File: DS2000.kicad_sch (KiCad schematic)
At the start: 56 parts, among them J1 USB-C, J2 SWD, J3 USB wire, SW1 MUTE, SW2 DEAFEN, SW3 DISCONNECT, SW4 BOOTSEL, SW5 RESET, U1 USBLC6-2SC6, U2 AP2112K-3.3, U3 RP2350A, U4 W25Q32JVSS, U5 74AHCT1G125, Y1 12MHz

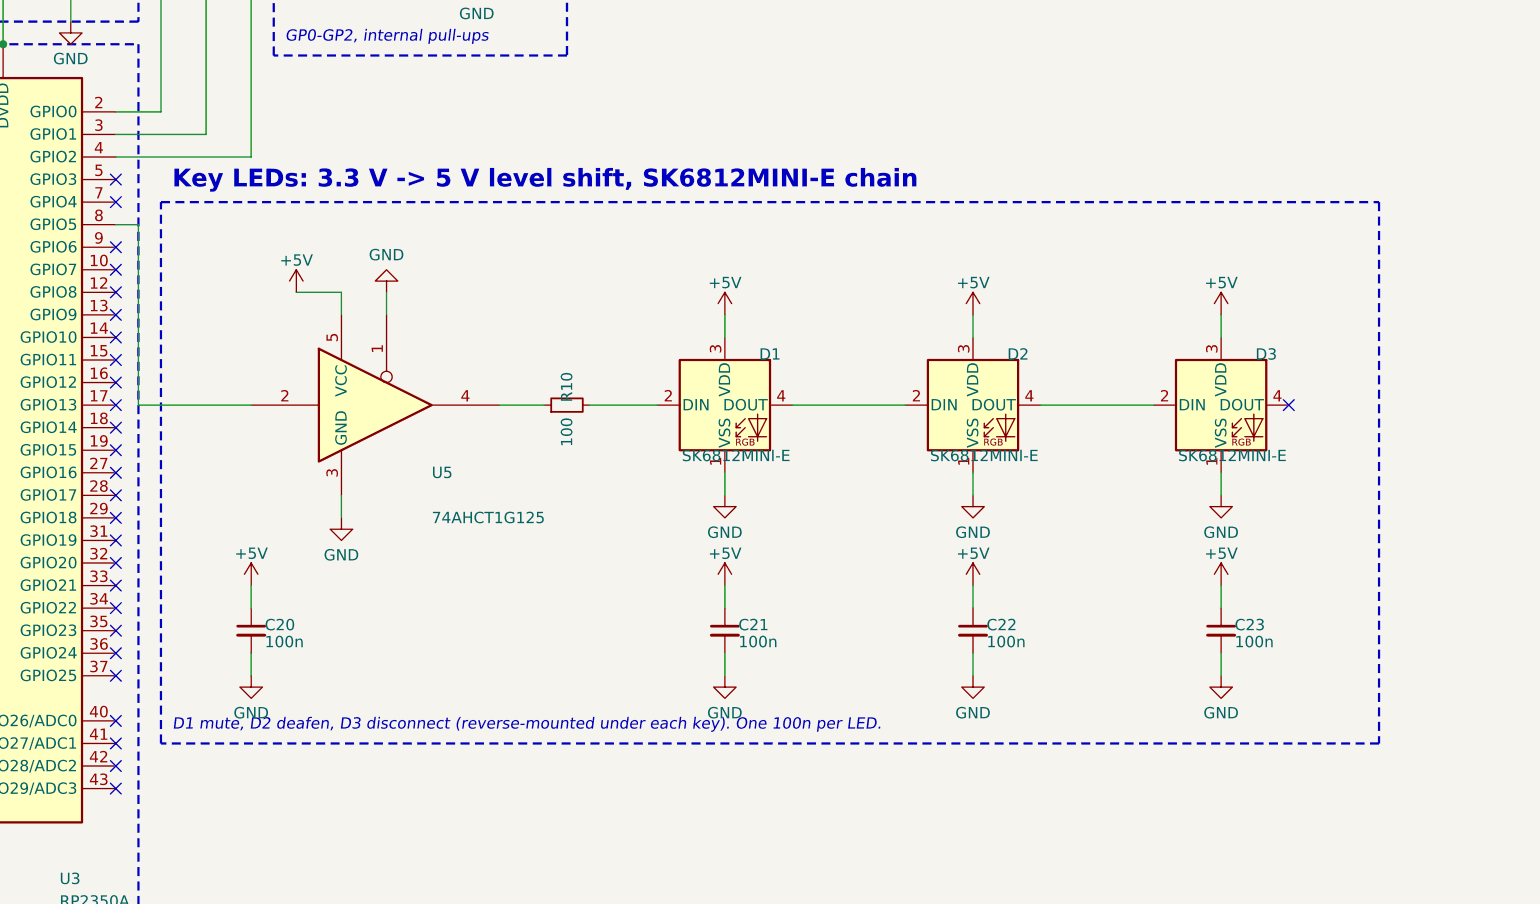
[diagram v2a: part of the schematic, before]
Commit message: feat: drop the LED under the disconnect key
Only mute and deafen carry state, so only they get an SK6812MINI-E. The chain is now U5 -> R10 ->
D1 (mute) -> D2 (deafen), which maps one-to-one onto the two colours the RGB message already
carries. D3 and its decoupling cap C23 are removed; ERC and the netlist check pass.
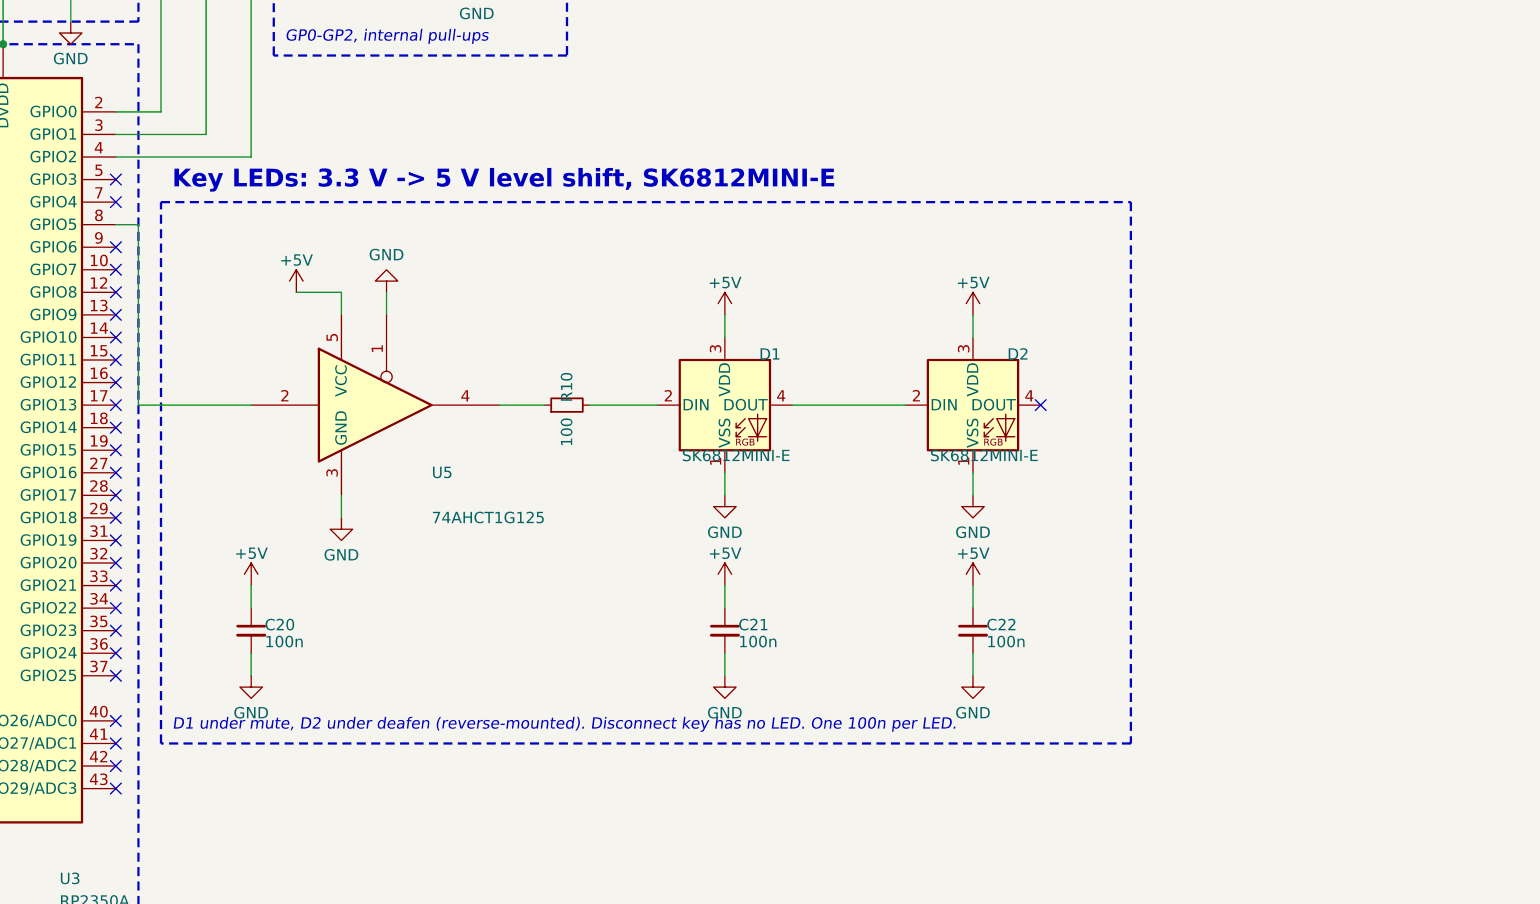
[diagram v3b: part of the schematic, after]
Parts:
- removed C18: 15p, Capacitor_SMD:C_0402_1005Metric, symbol Device:C_Small
- removed C22, C23: 100n, Capacitor_SMD:C_0402_1005Metric, symbol Device:C_Small
- removed C4: 4.7u, Capacitor_SMD:C_0402_1005Metric, symbol Device:C_Small
- removed D3: SK6812MINI-E, LED_SMD:LED_SK6812MINI-E_3.2x2.8mm_P1.5mm_ReverseMount, symbol LED:SK6812MINI-E
- removed H2: M2, MountingHole:MountingHole_2.2mm_M2_Pad_Via, symbol Mechanical:MountingHole_Pad
- removed R6: 1k, Resistor_SMD:R_0402_1005Metric, symbol Device:R_Small
- removed U2: AP2112K-3.3, Package_TO_SOT_SMD:SOT-23-5, symbol Regulator_Linear:AP2112K-3.3
- removed U3: RP2350A, Package_DFN_QFN:QFN-60-1EP_7x7mm_P0.4mm_EP3.4x3.4mm_ThermalVias, symbol MCU_RaspberryPi:RP2350A
- added C17: 15p, Capacitor_SMD:C_0402_1005Metric, symbol Device:C_Small
- added C20: 100n, Capacitor_SMD:C_0402_1005Metric, symbol Device:C_Small
- added D1: SK6812MINI-E, LED_SMD:LED_SK6812MINI-E_3.2x2.8mm_P1.5mm_ReverseMount, symbol LED:SK6812MINI-E
- added H1: M2, MountingHole:MountingHole_2.2mm_M2_Pad_Via, symbol Mechanical:MountingHole_Pad
- added R3: 27, Resistor_SMD:R_0402_1005Metric, symbol Device:R_Small
- added R9: 10k, Resistor_SMD:R_0402_1005Metric, symbol Device:R_Small
- added Y1: 12MHz, Crystal:Crystal_SMD_3225-4Pin_3.2x2.5mm, symbol Device:Crystal_GND24_Small
- C18: renamed from Y1; value 12MHz -> 15p; footprint Crystal:Crystal_SMD_3225-4Pin_3.2x2.5mm -> Capacitor_SMD:C_0402_1005Metric; symbol Device:Crystal_GND24_Small -> Device:C_Small; MPN ABM8-272-T3 -> (none); Manufacturer Abracon -> (none)
- C4: renamed from D2; value SK6812MINI-E -> 4.7u; footprint LED_SMD:LED_SK6812MINI-E_3.2x2.8mm_P1.5mm_ReverseMount -> Capacitor_SMD:C_0402_1005Metric; symbol LED:SK6812MINI-E -> Device:C_Small; MPN SK6812MINI-E -> (none); Manufacturer Opsco -> (none); Note Under the DEAFEN key -> VREG_VIN
- D2: renamed from D1; Note Under the MUTE key -> Under the DEAFEN key
- H2: renamed from R9; value 10k -> M2; footprint Resistor_SMD:R_0402_1005Metric -> MountingHole:MountingHole_2.2mm_M2_Pad_Via; symbol Device:R_Small -> Mechanical:MountingHole_Pad
- R6: renamed from C17; value 15p -> 1k; footprint Capacitor_SMD:C_0402_1005Metric -> Resistor_SMD:R_0402_1005Metric; symbol Device:C_Small -> Device:R_Small
- U2: renamed from R3; value 27 -> AP2112K-3.3; footprint Resistor_SMD:R_0402_1005Metric -> Package_TO_SOT_SMD:SOT-23-5; symbol Device:R_Small -> Regulator_Linear:AP2112K-3.3; MPN (none) -> AP2112K-3.3TRG1; Manufacturer (none) -> Diodes Inc; Note Place close to U3 -> (none)
- U3: renamed from H1; value M2 -> RP2350A; footprint MountingHole:MountingHole_2.2mm_M2_Pad_Via -> Package_DFN_QFN:QFN-60-1EP_7x7mm_P0.4mm_EP3.4x3.4mm_ThermalVias; symbol Mechanical:MountingHole_Pad -> MCU_RaspberryPi:RP2350A; MPN (none) -> RP2350A; Manufacturer (none) -> Raspberry Pi
- renumbered C20 to C21, C21 to C22
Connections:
- net +1V1: now also U3.23 (DVDD), U3.39 (DVDD), U3.50 (VREG_FB), U3.6 (DVDD)
- net +3V3: now also C4.1, U2.5 (VOUT), U3.1 (IOVDD), U3.11 (IOVDD), U3.20 (IOVDD), U3.30 (IOVDD), U3.38 (IOVDD), U3.44 (ADC_AVDD), U3.45 (IOVDD), U3.49 (VREG_VIN), U3.53 (USB_OTP_VDD), U3.54 (QSPI_IOVDD), R9.1; no longer H2.1
- net +5V: now also U2.1 (VIN), U2.3 (EN), C20.1, D1.3 (VDD); no longer C4.3 (VDD)
- net GND: now also C4.2, H2.1, U2.2 (GND), U3.47 (VREG_PGND), U3.61 (GND), C17.2, C20.2, D1.1 (VSS), H1.1, Y1.2 (G), Y1.4 (G); no longer C18.4 (G), C4.1 (VSS), R6.2, U3.1
- net RUN: now also U3.26 (RUN), R9.2; no longer H2.2
- net USB_CONN_DP: now also R3.1; no longer U2.1
- net USB_DM: now also U3.51 (USB_DM)
- net USB_DP: now also U3.52 (USB_DP), R3.2; no longer U2.2
- net at SW2.1: now also U3.3 (GPIO1)
- net at U5.2: now also U3.8 (GPIO5)
- net at C18.1, R6.1: now also Y1.3
- net at R7.2, R8.2, U4.1 (~{CS}): now also U3.60 (~{QSPI_SS})
- net at U4.2 (DO/IO_{1}): now also U3.59 (QSPI_SD1)
- net at U4.3 (~{WP}/IO_{2}): now also U3.58 (QSPI_SD2)
- net at U4.5 (DI/IO_{0}): now also U3.57 (QSPI_SD0)
- net at U4.6 (CLK): now also U3.56 (QSPI_SCLK)
- net at U4.7 (~{HOLD}/~{RESET}/IO_{3}): now also U3.55 (QSPI_SD3)
- net at L1.1: now also U3.48 (VREG_LX)
- net at C5.1, R5.2: now also U3.46 (VREG_AVDD)
- net at D2.4 (DOUT): no longer C4.2 (DIN)
- net at R10.2: now also D1.2 (DIN); no longer D2.2 (DIN)
- net at SW1.1: now also U3.2 (GPIO0)
- net at J2.1 (Pin_1): now also U3.24 (SWCLK)
- net at J2.3 (Pin_3): now also U3.25 (SWDIO)
- net at SW3.1: now also U3.4 (GPIO2)
- new net: C17.1, U3.21 (XIN), Y1.1
- new net: R6.2, U3.22 (XOUT)
- new net: D1.4 (DOUT), D2.2 (DIN)
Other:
- note added: "D1 under mute, D2 under deafen (reverse-mounted). Disconnect key has no LED. One 100n per LED."
- note added: "Key LEDs: 3.3 V -> 5 V level shift, SK6812MINI-E"
- note removed: "D1 mute, D2 deafen, D3 disconnect (reverse-mounted under each key). One 100n per LED."
- note removed: "Key LEDs: 3.3 V -> 5 V level shift, SK6812MINI-E chain"
- moved on the sheet: C21, C22, D2

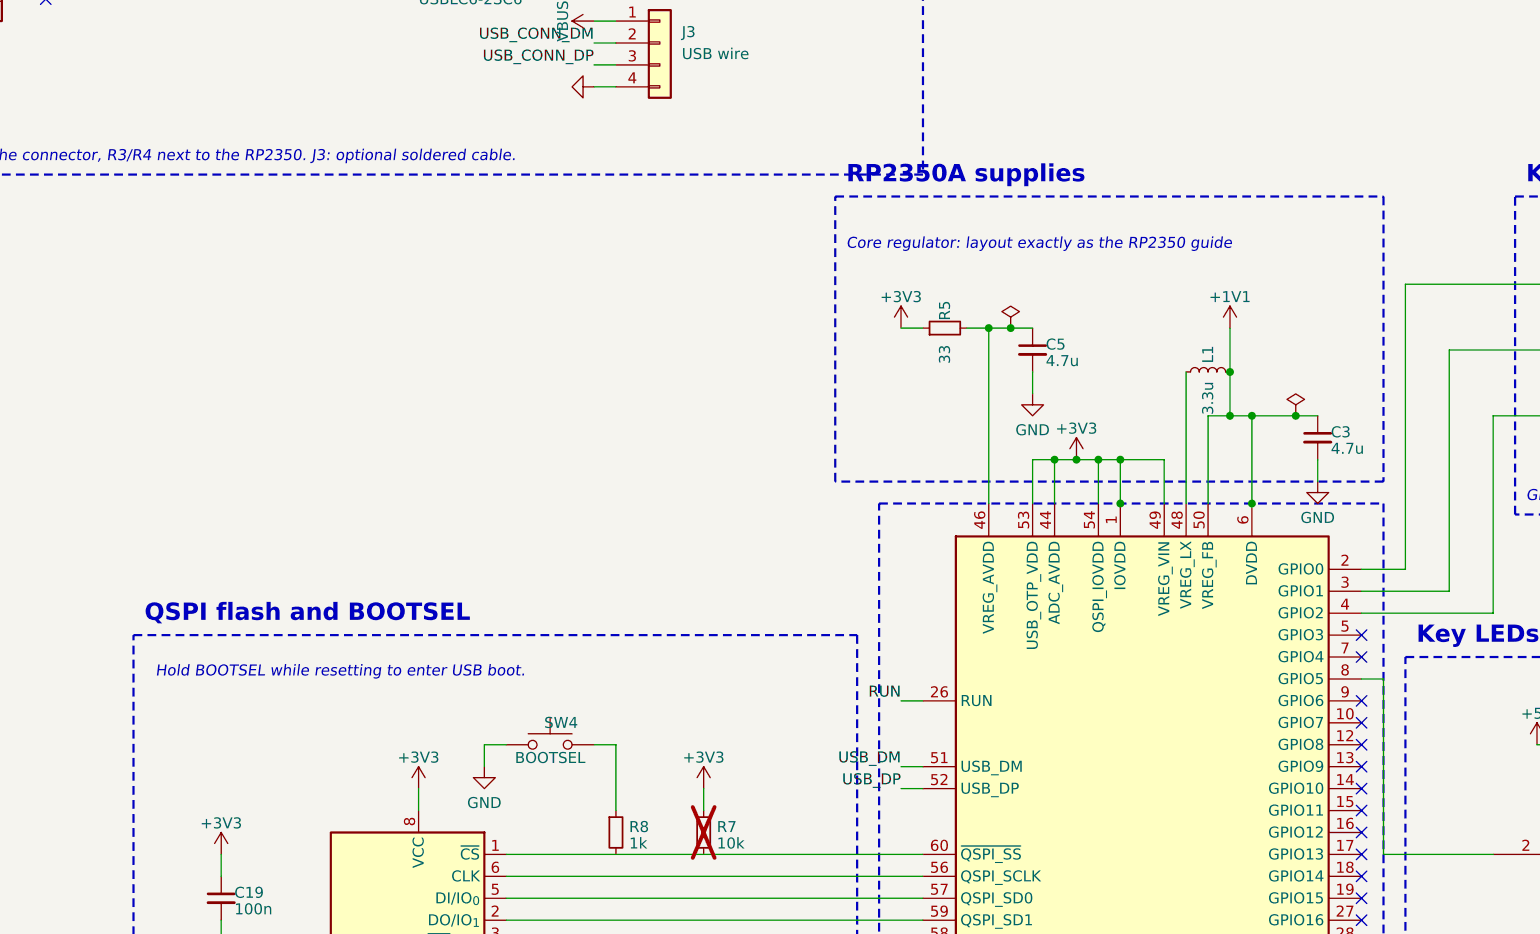
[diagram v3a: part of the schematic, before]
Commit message: feat: replace the BOOTSEL button with a pair of bridgeable pads
BOOTSEL is only needed to recover a board whose firmware no longer enumerates, so a tactile switch
on the visible face is not worth its place. JP1 is an open solder jumper: bridging its two pads
with tweezers while plugging in USB pulls QSPI_SS low through R8 and the RP2350A starts in USB boot
mode. Not in the BOM. ERC and the netlist check pass.
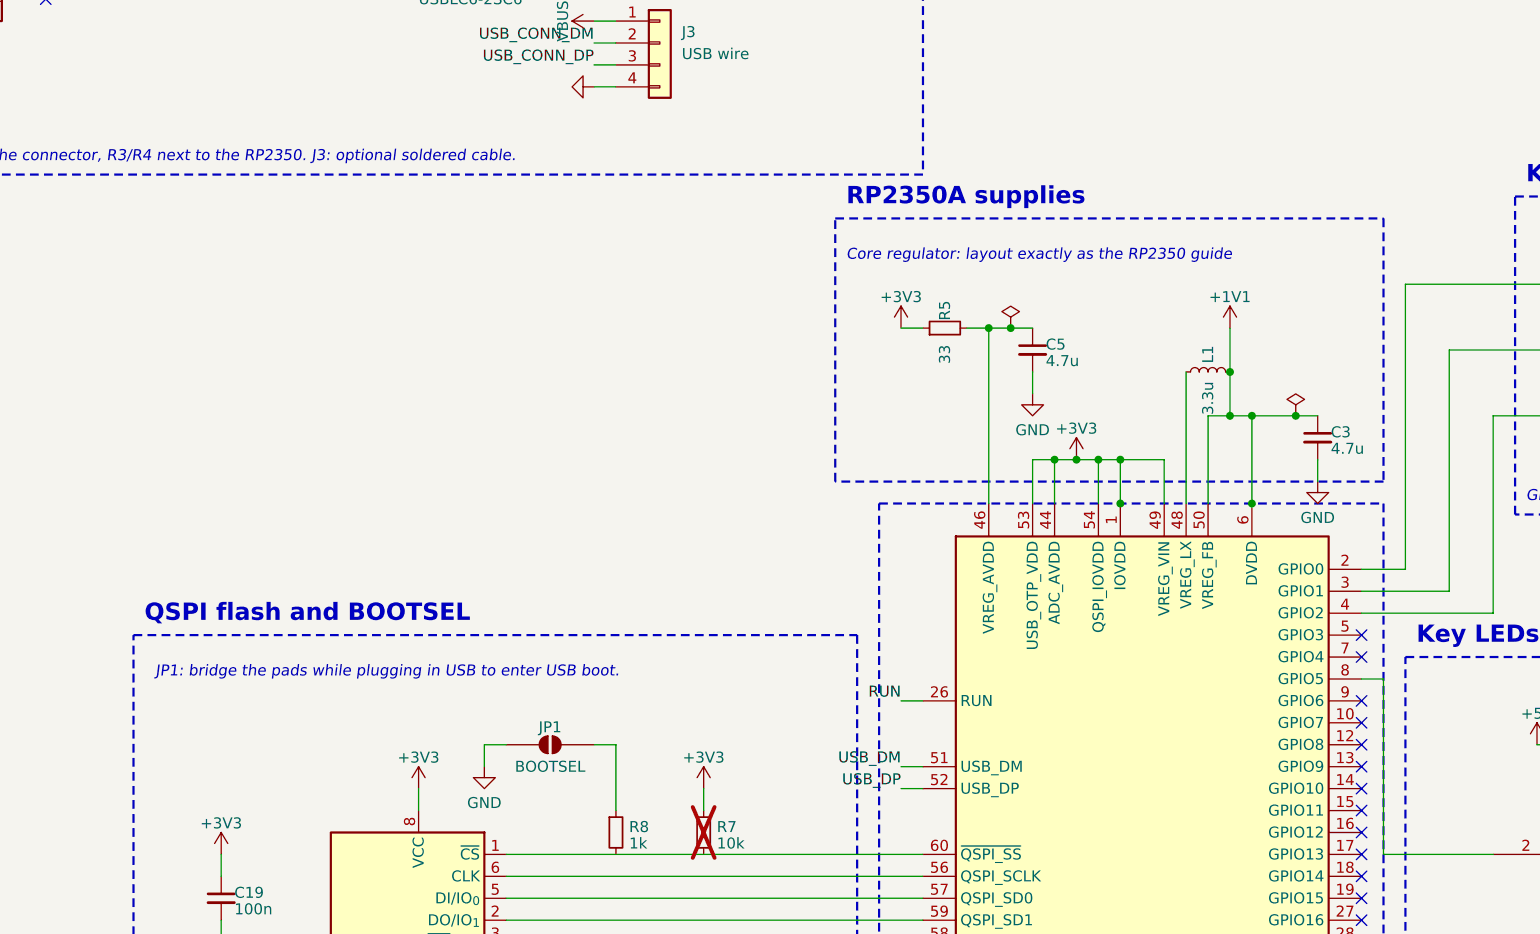
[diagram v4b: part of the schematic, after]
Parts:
- JP1: renamed from SW4; footprint Button_Switch_SMD:SW_Push_1P1T_XKB_TS-1187A -> Jumper:SolderJumper-2_P1.3mm_Open_RoundedPad1.0x1.5mm; symbol Switch:SW_Push -> Jumper:SolderJumper_2_Open; MPN TS-1187A-B-A-B -> (none); Manufacturer XKB -> (none); Note (none) -> Bridge with tweezers while plugging in USB (or pressing RES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; now left out of the parts list
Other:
- note added: "JP1: bridge the pads while plugging in USB to enter USB boot."
- note removed: "Hold BOOTSEL while resetting to enter USB boot."
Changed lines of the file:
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@@
 	(polyline
 		(pts
-			(xy 147.32 114.3) (xy 210.82 114.3) (xy 210.82 147.32) (xy 147.32 147.32) (xy 147.32 114.3)
+			(xy 147.32 116.84) (xy 210.82 116.84) (xy 210.82 147.32) (xy 147.32 147.32) (xy 147.32 116.84)
 		)
 		(stroke
@@
 	(text "Core regulator: layout exactly as the RP2350 guide"
 		(exclude_from_sim no)
-		(at 148.59 120.65 0)
+		(at 148.59 121.92 0)
 		(effects
 			(font
@@
 	(text "RP2350A supplies"
 		(exclude_from_sim no)
-		(at 148.59 113.03 0)
+		(at 148.59 115.57 0)
 		(effects
 			(font
@@
 		)
 	)
-	(text "Hold BOOTSEL while resetting to enter USB boot."
+	(text "JP1: bridge the pads while plugging in USB to enter USB boot."
 		(exclude_from_sim no)
 		(at 68.58 170.18 0)
@@
 	)
 	(symbol
-		(lib_id "Switch:SW_Push")
+		(lib_id "Jumper:SolderJumper_2_Open")
 		(at 114.3 177.8 0)
 		(unit 1)
 		(body_style 1)
 		(exclude_from_sim no)
-		(in_bom yes)
+		(in_bom no)
 		(on_board yes)
 		(in_pos_files yes)
 		(dnp no)
-		(property "Reference" "SW4"
-			(at 115.57 175.26 0)
+		(property "Reference" "JP1"
+			(at 114.3 175.768 0)
 			(show_name no)
 			(do_not_autoplace no)
@@
 		)
 		(property "Value" "BOOTSEL"
-			(at 114.3 179.324 0)
+			(at 114.3 180.34 0)
 			(show_name no)
 			(do_not_autoplace no)
@@
 			)
 		)
-		(property "Footprint" "Button_Switch_SMD:SW_Push_1P1T_XKB_TS-1187A"
+		(property "Footprint" "Jumper:SolderJumper-2_P1.3mm_Open_RoundedPad1.0x1.5mm"
 			(at 114.3 177.8 0)
 			(hide yes)
@@
 			)
 		)
-		(property "MPN" "TS-1187A-B-A-B"
-			(at 114.3 177.8 0)
-			(hide yes)
-			(show_name no)
-			(do_not_autoplace no)
-			(effects
-				(font
-					(size 1.27 1.27)
-				)
-			)
-		)
-		(property "Manufacturer" "XKB"
+		(property "Note" "Bridge with tweezers while plugging in USB (or pressing RESET) to enter USB boot"
 			(at 114.3 177.8 0)
 			(hide yes)
@@
 			(project ""
 				(path "/defea174-d404-5f0f-95d3-26e7103e2a73"
-					(reference "SW4")
+					(reference "JP1")
 					(unit 1)
 				)
